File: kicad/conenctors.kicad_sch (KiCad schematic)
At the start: 8 parts, among them J3 USB4105-GF-A, J6 Conn_02x12_Counter_Clockwise

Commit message: Connected all remaining unconnected pins
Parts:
- removed J6: Conn_02x12_Counter_Clockwise, Connector_JST:JST_PHD_B24B-PHDSS_2x12_P2.00mm_Vertical, symbol Connector_Generic:Conn_02x12_Counter_Clockwise
- added J?: Conn_02x20_Odd_Even, Connector_JST:JST_PHD_B24B-PHDSS_2x12_P2.00mm_Vertical, symbol Connector_Generic:Conn_02x20_Odd_Even
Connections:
- net CAN_HI: now also J?.2 (Pin_2), J?.4 (Pin_4)
- net CAN_LO: now also J?.1 (Pin_1), J?.3 (Pin_3)
- net GND: now also J?.15 (Pin_15), J?.16 (Pin_16), J?.36 (Pin_36), J?.8 (Pin_8)
- net VIN_12V: now also J?.6 (Pin_6)
- new net +3V3: J?.11 (Pin_11), J?.13 (Pin_13)
- new net +5V: J?.12 (Pin_12), J?.14 (Pin_14)
- new net CONN_15_A4: J?.23 (Pin_23)
- new net CONN_16_A5: J?.25 (Pin_25)
- new net CONN_17_A6: J?.27 (Pin_27)
- new net CONN_18_A7: J?.29 (Pin_29)
- new net CONN_19_A8: J?.31 (Pin_31)
- new net CONN_20_A9: J?.33 (Pin_33)
- new net CONN_21_A10: J?.35 (Pin_35)
- new net CONN_22_A11: J?.37 (Pin_37)
- new net GPIO_1: J?.18 (Pin_18)
- new net GPIO_10: J?.38 (Pin_38)
- new net GPIO_11: J?.40 (Pin_40)
- new net GPIO_12_A1: J?.17 (Pin_17)
- new net GPIO_13_A2: J?.19 (Pin_19)
- new net GPIO_14_A3: J?.21 (Pin_21)
- new net GPIO_2: J?.20 (Pin_20)
- new net GPIO_23: J?.39 (Pin_39)
- new net GPIO_3: J?.22 (Pin_22)
- new net GPIO_4: J?.24 (Pin_24)
- new net GPIO_5: J?.26 (Pin_26)
- new net GPIO_6: J?.28 (Pin_28)
- new net GPIO_7: J?.30 (Pin_30)
- new net GPIO_8: J?.32 (Pin_32)
- new net GPIO_9: J?.34 (Pin_34)
- new net GPIO_RESET: J?.7 (Pin_7)
- new net SWCIK: J?.9 (Pin_9)
- new net SWDIO: J?.10 (Pin_10)
- new net VIN_5V: J?.5 (Pin_5)
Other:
- note added: "NOTE: ONLY ON PLUS BOARDS"
- note added: "PLUS: 40 pin connector 12 digital 11 analog 10 power (2 3V3 out, 2 5V out, 4 GND, 1 12V in, 1 5V in) 2 debug 1 reset 4 CAN"
- note added: "REGULAR: 30 pin connector 7 digital 7 analog 9 power (2 3V3 out, 2 5V out, 3 GND, 1 12V in, 1 5V in) 2 debug 1 reset 4 CAN"
- note removed: "PLUS: 40 pin connector 15 digital 8 analog/digital 3 analog 10 power (2 3V3 out, 2 5V out, 4 GND, 1 12V in, 1 5V in) 2 debug 1 reset"
- note removed: "REGULAR: 30 pin connector 10 digital 7 analog 10 power (2 3V3 out, 2 5V out, 4 GND, 1 12V in, 1 5V in) 2 debug 1 reset"

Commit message: Updated schematic with various changes
Increased size of small components
Updated title/spec sheet
Cleaned footprints
Other small changes as well
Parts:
- R10: renamed from R6; footprint personal:R_0201_0603Metric -> personal:R_0402_1005Metric
- R9: renamed from R5; footprint personal:R_0201_0603Metric -> personal:R_0402_1005Metric
- gave numbers to parts that had none: 1
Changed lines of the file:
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@@
   (symbol (lib_id "power:+5V") (at 195.58 91.44 270) (unit 1)
     (in_bom yes) (on_board yes) (fields_autoplaced)
-    (property "Reference" "#PWR?" (id 0) (at 191.77 91.44 0)
+    (property "Reference" "#PWR064" (id 0) (at 191.77 91.44 0)
       (effects (font (size 1.27 1.27)) hide)
     )
@@
   (symbol (lib_id "power:GND") (at 71.12 91.44 0) (unit 1)
     (in_bom yes) (on_board yes) (fields_autoplaced)
-    (property "Reference" "#PWR015" (id 0) (at 71.12 97.79 0)
+    (property "Reference" "#PWR061" (id 0) (at 71.12 97.79 0)
       (effects (font (size 1.27 1.27)) hide)
     )
@@
   (symbol (lib_id "power:+5V") (at 195.58 88.9 270) (unit 1)
     (in_bom yes) (on_board yes) (fields_autoplaced)
-    (property "Reference" "#PWR?" (id 0) (at 191.77 88.9 0)
+    (property "Reference" "#PWR060" (id 0) (at 191.77 88.9 0)
       (effects (font (size 1.27 1.27)) hide)
     )
@@
   (symbol (lib_id "power:GND") (at 182.88 86.36 270) (unit 1)
     (in_bom yes) (on_board yes) (fields_autoplaced)
-    (property "Reference" "#PWR?" (id 0) (at 176.53 86.36 0)
+    (property "Reference" "#PWR057" (id 0) (at 176.53 86.36 0)
       (effects (font (size 1.27 1.27)) hide)
     )
@@
   (symbol (lib_id "power:GND") (at 195.58 86.36 90) (unit 1)
     (in_bom yes) (on_board yes) (fields_autoplaced)
-    (property "Reference" "#PWR?" (id 0) (at 201.93 86.36 0)
+    (property "Reference" "#PWR058" (id 0) (at 201.93 86.36 0)
       (effects (font (size 1.27 1.27)) hide)
     )
@@
   (symbol (lib_id "Device:R") (at 129.54 86.36 180) (unit 1)
     (in_bom yes) (on_board yes)
-    (property "Reference" "R6" (id 0) (at 132.08 85.0899 0)
+    (property "Reference" "R10" (id 0) (at 132.08 85.0899 0)
       (effects (font (size 1.27 1.27)) (justify right))
     )
@@
       (effects (font (size 1.27 1.27)) (justify right))
     )
-    (property "Footprint" "personal:R_0201_0603Metric" (id 2) (at 131.318 86.36 90)
+    (property "Footprint" "personal:R_0402_1005Metric" (id 2) (at 131.318 86.36 90)
       (effects (font (size 1.27 1.27)) hide)
     )
@@
   (symbol (lib_id "Connector_Generic:Conn_02x20_Odd_Even") (at 187.96 81.28 0) (mirror x) (unit 1)
     (in_bom yes) (on_board yes)
-    (property "Reference" "J?" (id 0) (at 189.23 48.26 0))
+    (property "Reference" "J2" (id 0) (at 189.23 48.26 0))
     (property "Value" "Conn_02x20_Odd_Even" (id 1) (at 189.23 50.8 0))
     (property "Footprint" "Connector_JST:JST_PHD_B24B-PHDSS_2x12_P2.00mm_Vertical" (id 2) (at 187.96 81.28 0)
@@
   (symbol (lib_id "power:GND") (at 123.19 97.79 0) (unit 1)
     (in_bom yes) (on_board yes)
-    (property "Reference" "#PWR017" (id 0) (at 123.19 104.14 0)
+    (property "Reference" "#PWR066" (id 0) (at 123.19 104.14 0)
       (effects (font (size 1.27 1.27)) hide)
     )
@@
   (symbol (lib_id "Device:R") (at 71.12 86.36 0) (unit 1)
     (in_bom yes) (on_board yes)
-    (property "Reference" "R5" (id 0) (at 64.77 85.09 0)
+    (property "Reference" "R9" (id 0) (at 64.77 85.09 0)
       (effects (font (size 1.27 1.27)) (justify left))
     )
@@
       (effects (font (size 1.27 1.27)) (justify left))
     )
-    (property "Footprint" "personal:R_0201_0603Metric" (id 2) (at 69.342 86.36 90)
+    (property "Footprint" "personal:R_0402_1005Metric" (id 2) (at 69.342 86.36 90)
       (effects (font (size 1.27 1.27)) hide)
     )
@@
   (symbol (lib_id "power:GND") (at 69.85 132.08 0) (unit 1)
     (in_bom yes) (on_board yes) (fields_autoplaced)
-    (property "Reference" "#PWR018" (id 0) (at 69.85 138.43 0)
+    (property "Reference" "#PWR067" (id 0) (at 69.85 138.43 0)
       (effects (font (size 1.27 1.27)) hide)
     )
@@
   (symbol (lib_id "power:GND") (at 195.58 96.52 90) (unit 1)
     (in_bom yes) (on_board yes) (fields_autoplaced)
-    (property "Reference" "#PWR?" (id 0) (at 201.93 96.52 0)
+    (property "Reference" "#PWR065" (id 0) (at 201.93 96.52 0)
       (effects (font (size 1.27 1.27)) hide)
     )
@@
   (symbol (lib_id "power:+3V3") (at 182.88 88.9 90) (unit 1)
     (in_bom yes) (on_board yes) (fields_autoplaced)
-    (property "Reference" "#PWR?" (id 0) (at 186.69 88.9 0)
+    (property "Reference" "#PWR059" (id 0) (at 186.69 88.9 0)
       (effects (font (size 1.27 1.27)) hide)
     )
@@
   (symbol (lib_id "power:GND") (at 195.58 60.96 90) (unit 1)
     (in_bom yes) (on_board yes) (fields_autoplaced)
-    (property "Reference" "#PWR?" (id 0) (at 201.93 60.96 0)
+    (property "Reference" "#PWR056" (id 0) (at 201.93 60.96 0)
       (effects (font (size 1.27 1.27)) hide)
     )
@@
   (symbol (lib_id "power:GND") (at 129.54 91.44 0) (unit 1)
     (in_bom yes) (on_board yes)
-    (property "Reference" "#PWR016" (id 0) (at 129.54 97.79 0)
+    (property "Reference" "#PWR062" (id 0) (at 129.54 97.79 0)
       (effects (font (size 1.27 1.27)) hide)
     )
@@
   (symbol (lib_id "power:+3V3") (at 182.88 91.44 90) (unit 1)
     (in_bom yes) (on_board yes) (fields_autoplaced)
-    (property "Reference" "#PWR?" (id 0) (at 186.69 91.44 0)
-      (effects (font (size 1.27 1.27)) hide)
-    )
+    (property "Reference" "#PWR063" (id 0) (at 186.69 91.44 0)
+      (effects (font (size 1.27 1.27)) hide)
+    )

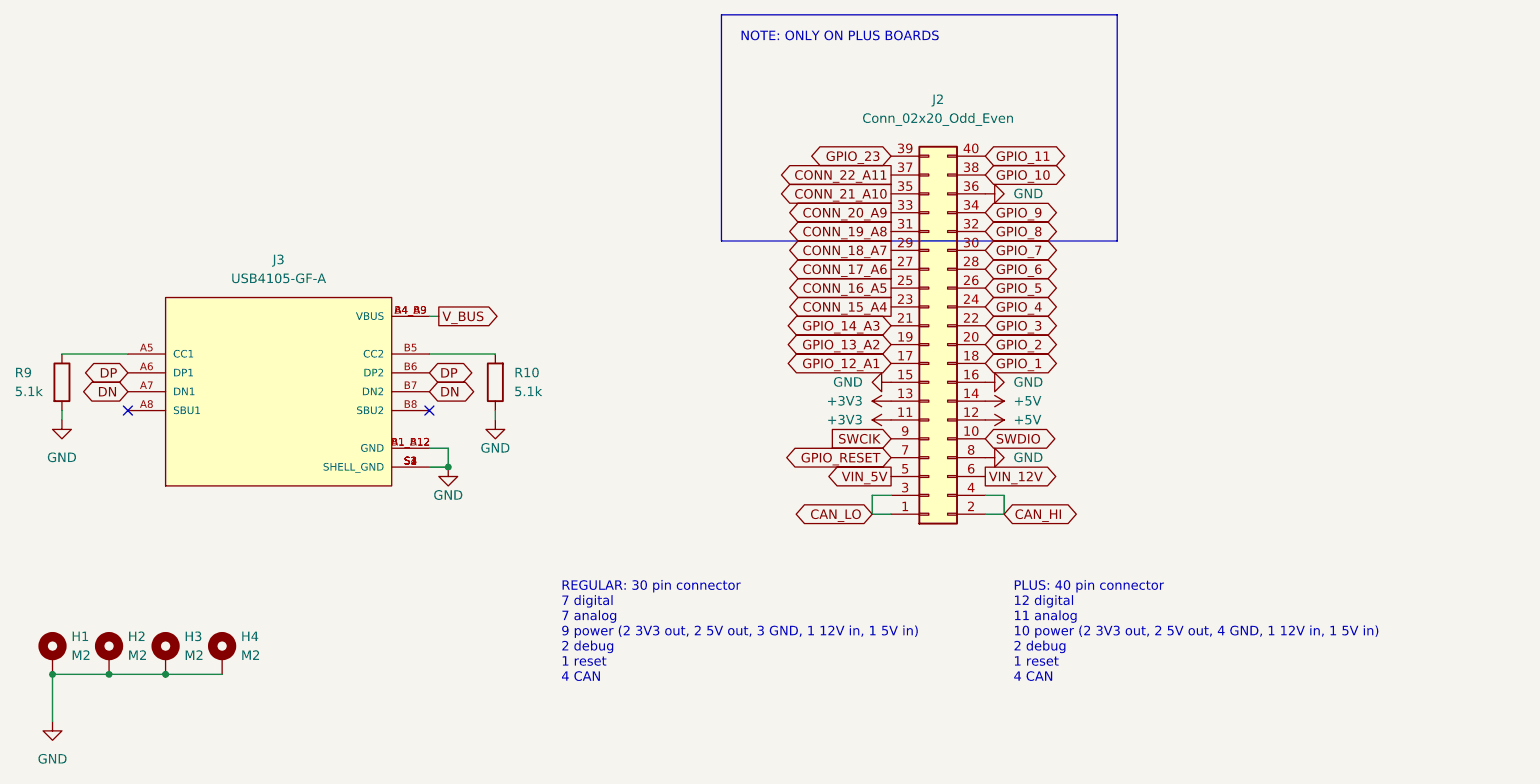
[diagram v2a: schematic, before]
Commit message: Changed pinout on main pcb connector
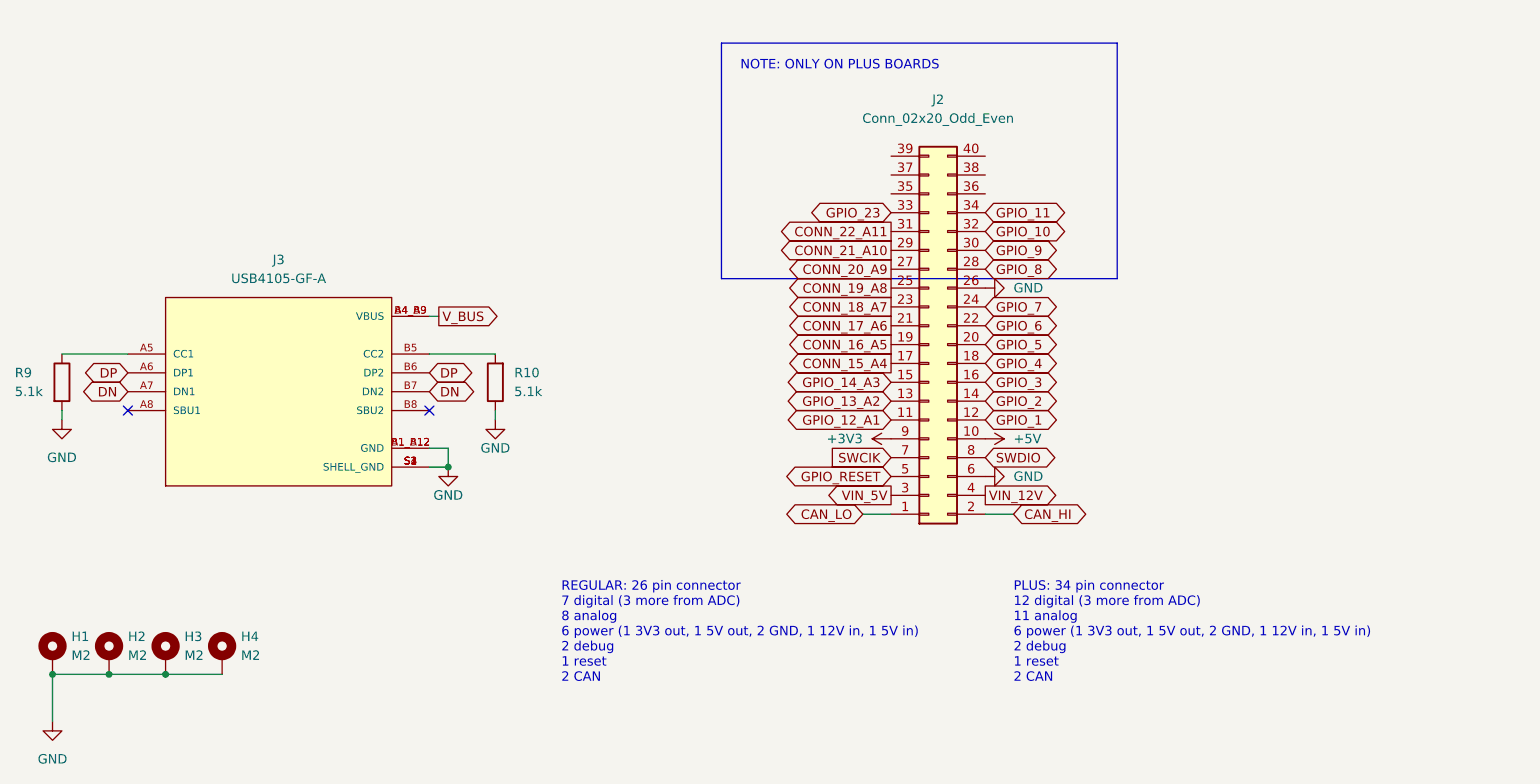
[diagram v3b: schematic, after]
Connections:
- net +3V3: now also J2.9 (Pin_9); no longer J2.11 (Pin_11), J2.13 (Pin_13)
- net +5V: now also J2.10 (Pin_10); no longer J2.12 (Pin_12), J2.14 (Pin_14)
- net CAN_HI: no longer J2.4 (Pin_4)
- net CAN_LO: no longer J2.3 (Pin_3)
- net CONN_15_A4: now also J2.17 (Pin_17); no longer J2.23 (Pin_23)
- net CONN_16_A5: now also J2.19 (Pin_19); no longer J2.25 (Pin_25)
- net CONN_17_A6: now also J2.21 (Pin_21); no longer J2.27 (Pin_27)
- net CONN_18_A7: now also J2.23 (Pin_23); no longer J2.29 (Pin_29)
- net CONN_19_A8: now also J2.25 (Pin_25); no longer J2.31 (Pin_31)
- net CONN_20_A9: now also J2.27 (Pin_27); no longer J2.33 (Pin_33)
- net CONN_21_A10: now also J2.29 (Pin_29); no longer J2.35 (Pin_35)
- net CONN_22_A11: now also J2.31 (Pin_31); no longer J2.37 (Pin_37)
- net GND: now also J2.26 (Pin_26), J2.6 (Pin_6); no longer J2.15 (Pin_15), J2.16 (Pin_16), J2.36 (Pin_36), J2.8 (Pin_8)
- net GPIO_1: now also J2.12 (Pin_12); no longer J2.18 (Pin_18)
- net GPIO_10: now also J2.32 (Pin_32); no longer J2.38 (Pin_38)
- net GPIO_11: now also J2.34 (Pin_34); no longer J2.40 (Pin_40)
- net GPIO_12_A1: now also J2.11 (Pin_11); no longer J2.17 (Pin_17)
- net GPIO_13_A2: now also J2.13 (Pin_13); no longer J2.19 (Pin_19)
- net GPIO_14_A3: now also J2.15 (Pin_15); no longer J2.21 (Pin_21)
- net GPIO_2: now also J2.14 (Pin_14); no longer J2.20 (Pin_20)
- net GPIO_23: now also J2.33 (Pin_33); no longer J2.39 (Pin_39)
- net GPIO_3: now also J2.16 (Pin_16); no longer J2.22 (Pin_22)
- net GPIO_4: now also J2.18 (Pin_18); no longer J2.24 (Pin_24)
- net GPIO_5: now also J2.20 (Pin_20); no longer J2.26 (Pin_26)
- net GPIO_6: now also J2.22 (Pin_22); no longer J2.28 (Pin_28)
- net GPIO_7: now also J2.24 (Pin_24); no longer J2.30 (Pin_30)
- net GPIO_8: now also J2.28 (Pin_28); no longer J2.32 (Pin_32)
- net GPIO_9: now also J2.30 (Pin_30); no longer J2.34 (Pin_34)
- net GPIO_RESET: now also J2.5 (Pin_5); no longer J2.7 (Pin_7)
- net SWCIK: now also J2.7 (Pin_7); no longer J2.9 (Pin_9)
- net SWDIO: now also J2.8 (Pin_8); no longer J2.10 (Pin_10)
- net VIN_12V: now also J2.4 (Pin_4); no longer J2.6 (Pin_6)
- net VIN_5V: now also J2.3 (Pin_3); no longer J2.5 (Pin_5)
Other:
- note added: "PLUS: 34 pin connector 12 digital (3 more from ADC) 11 analog 6 power (1 3V3 out, 1 5V out, 2 GND, 1 12V in, 1 5V in) 2 debug 1 reset 2 CAN"
- note added: "REGULAR: 26 pin connector 7 digital (3 more from ADC) 8 analog 6 power (1 3V3 out, 1 5V out, 2 GND, 1 12V in, 1 5V in) 2 debug 1 reset 2 CAN"
- note removed: "PLUS: 40 pin connector 12 digital 11 analog 10 power (2 3V3 out, 2 5V out, 4 GND, 1 12V in, 1 5V in) 2 debug 1 reset 4 CAN"
- note removed: "REGULAR: 30 pin connector 7 digital 7 analog 9 power (2 3V3 out, 2 5V out, 3 GND, 1 12V in, 1 5V in) 2 debug 1 reset 4 CAN"
